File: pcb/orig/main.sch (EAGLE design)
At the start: 23 parts, among them Q1 MOSFET-NCHANNEL2N7000

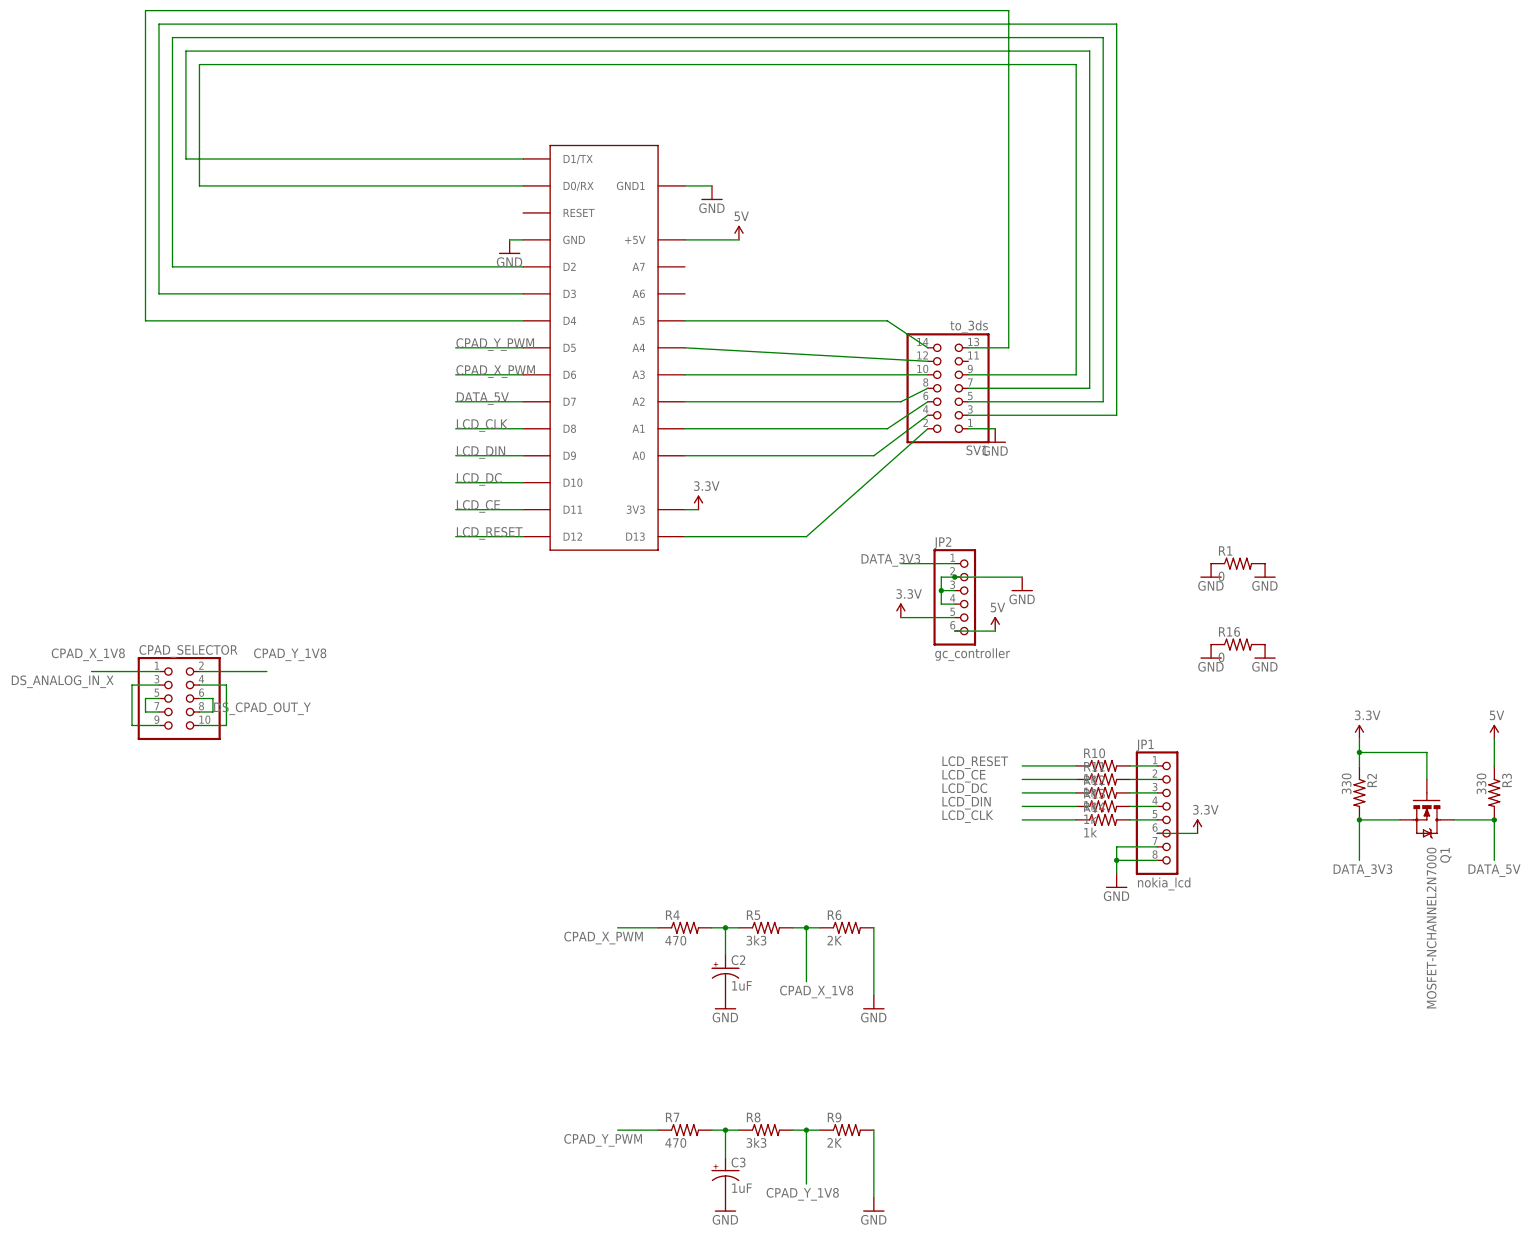
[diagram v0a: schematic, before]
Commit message: built-in c-pad selector
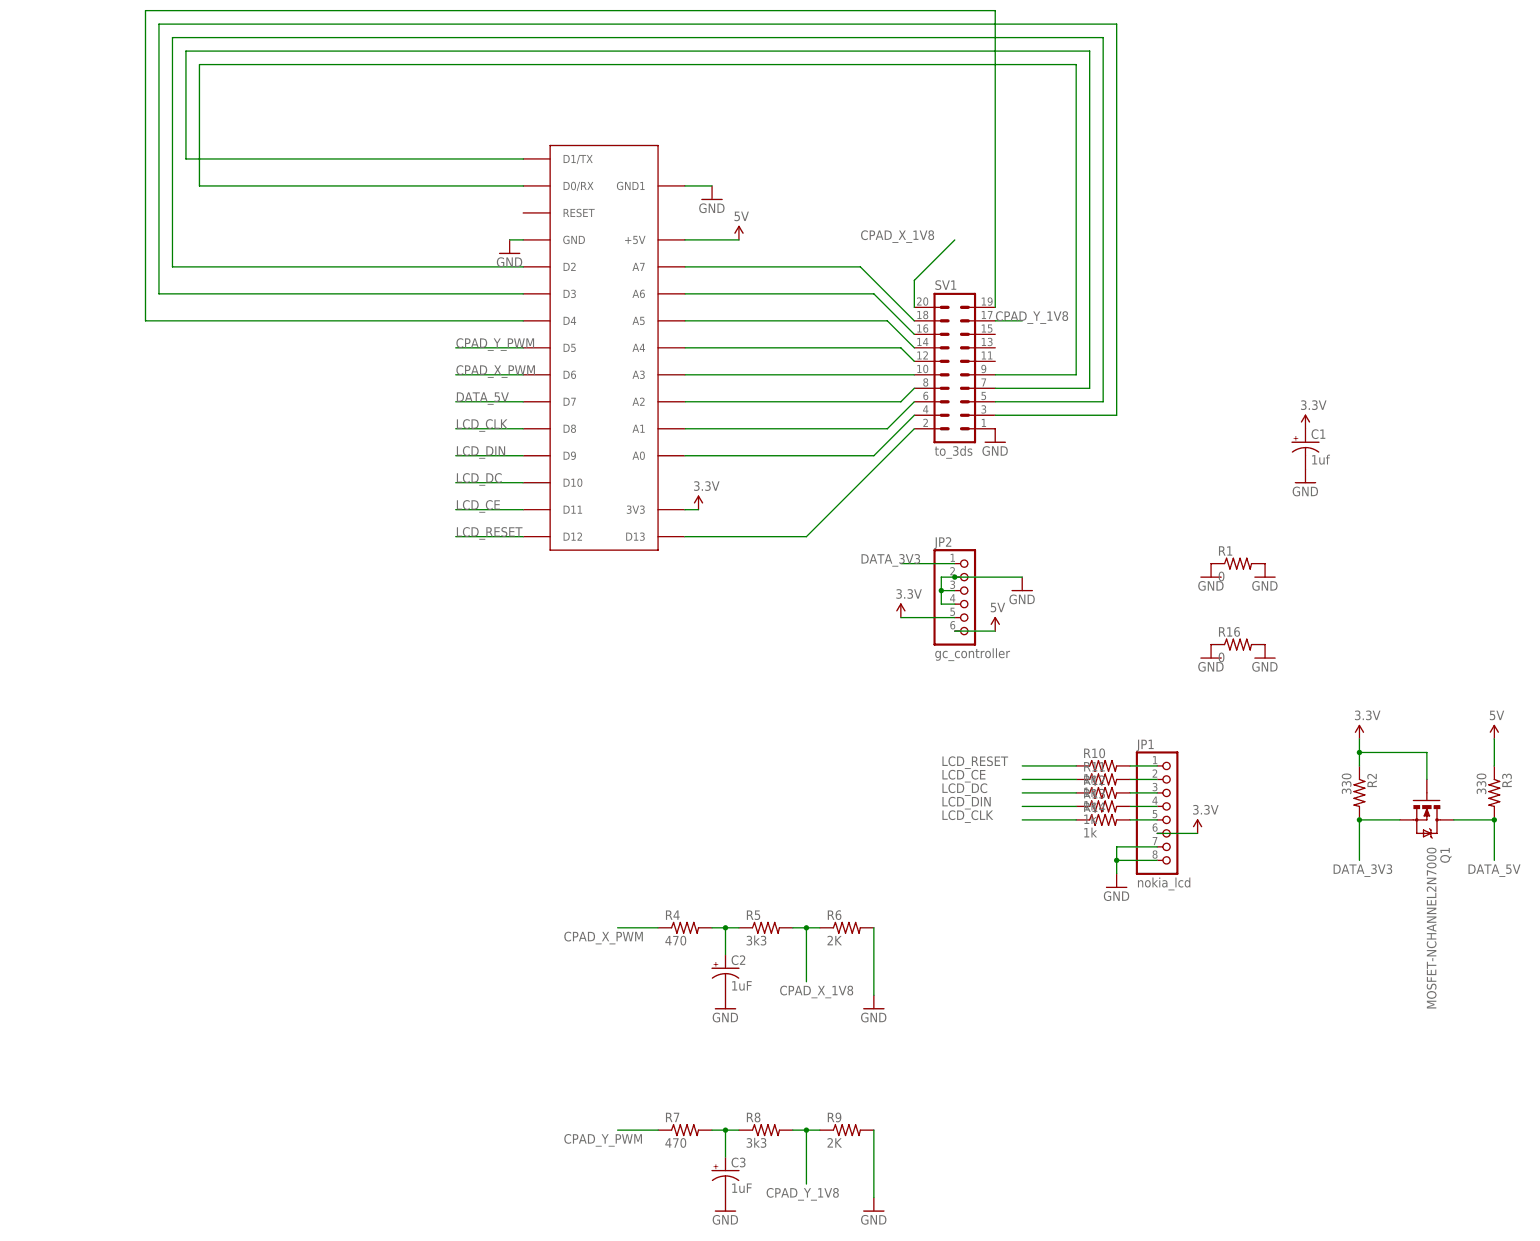
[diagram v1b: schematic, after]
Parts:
- removed CPAD_SELECTOR: (no value), pinhead:PINHD-2X5
- added C1: 1uf, SparkFun-Capacitors:CAP_POLPTH2
- SV1: device pinhead:PINHD-2X7 -> con-lstb:MA10-2
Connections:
- removed net DS_ANALOG_IN_X: CPAD_SELECTOR.3, CPAD_SELECTOR.9
- removed net DS_ANALOG_IN_Y: CPAD_SELECTOR.10, CPAD_SELECTOR.4
- removed net DS_CPAD_OUTX: CPAD_SELECTOR.5, CPAD_SELECTOR.7
- removed net DS_CPAD_OUT_Y: CPAD_SELECTOR.6, CPAD_SELECTOR.8
- new net N$15: SV1.16, U$1.A6
- new net N$16: SV1.18, U$1.A7
- net 3.3V: now also C1.+
- net CPAD_X_1V8: now also SV1.20; no longer CPAD_SELECTOR.1
- net CPAD_Y_1V8: now also SV1.17; no longer CPAD_SELECTOR.2
- net GND: now also C1.-
- net N$18: now also SV1.19; no longer SV1.13
